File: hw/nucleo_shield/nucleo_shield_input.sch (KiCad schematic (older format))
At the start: 57 parts, among them P1 CONN_INH1, P17 CONN_INH3, P5 CONN_INH2, U15 LTV-847, U16 LTV-847, U3 LTV-847, U4 LTV-847, U5 LTV-847, U6 LTV-847

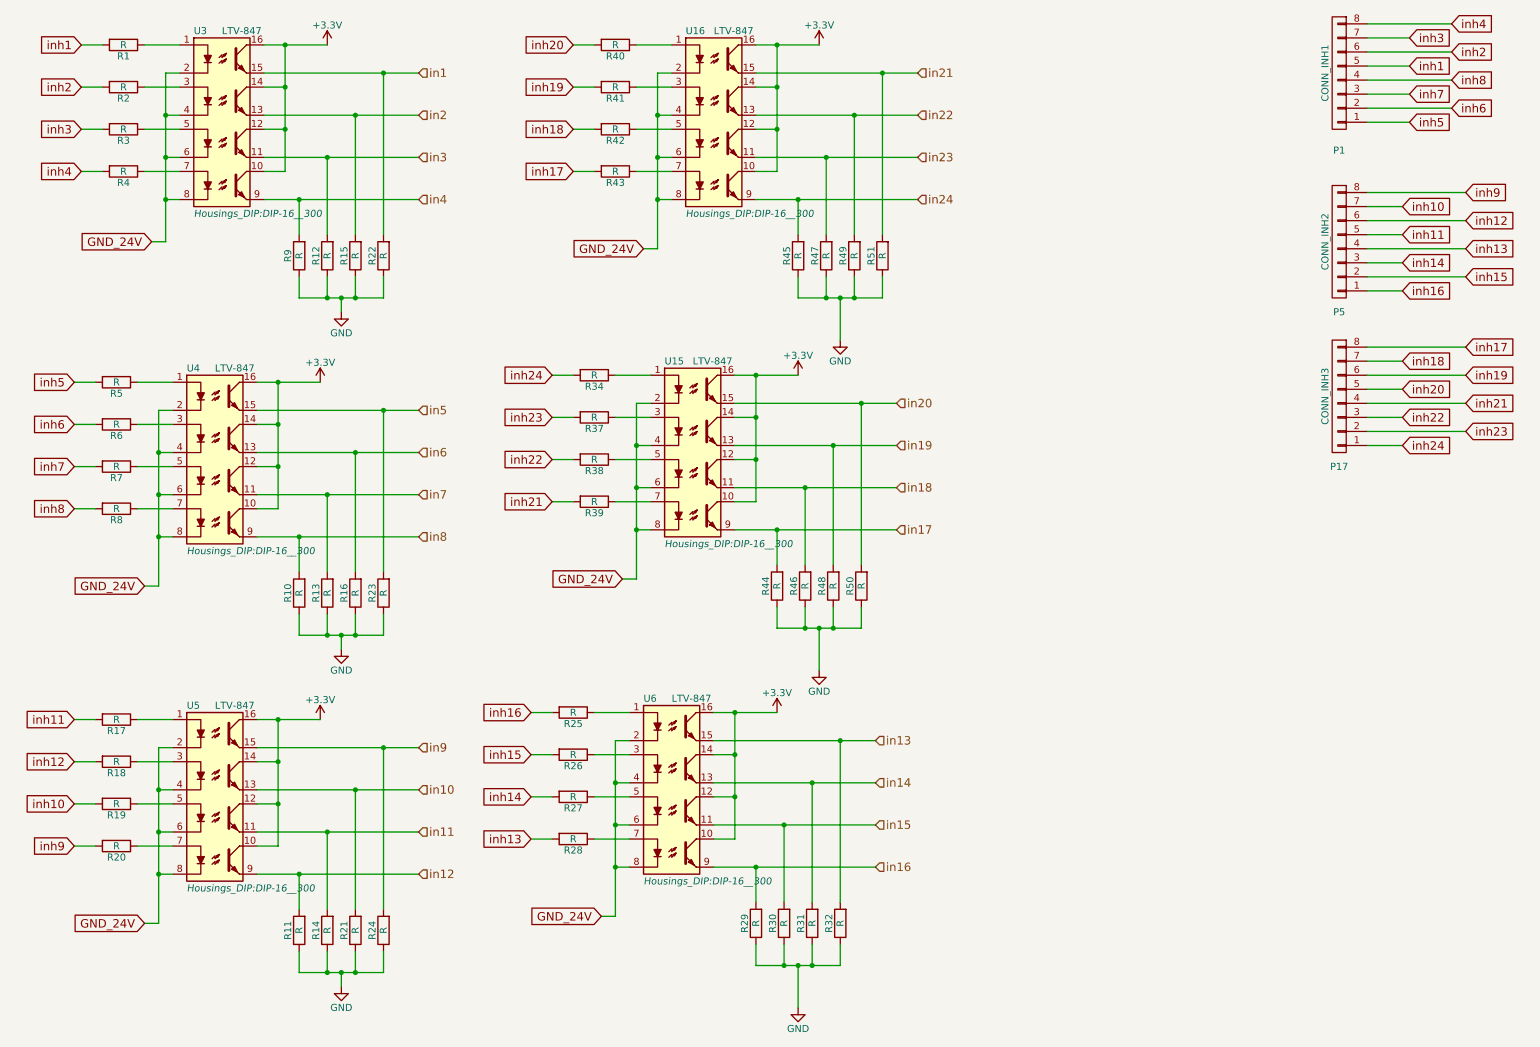
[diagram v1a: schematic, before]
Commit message: Nucleo: Remove input pullup on pcf
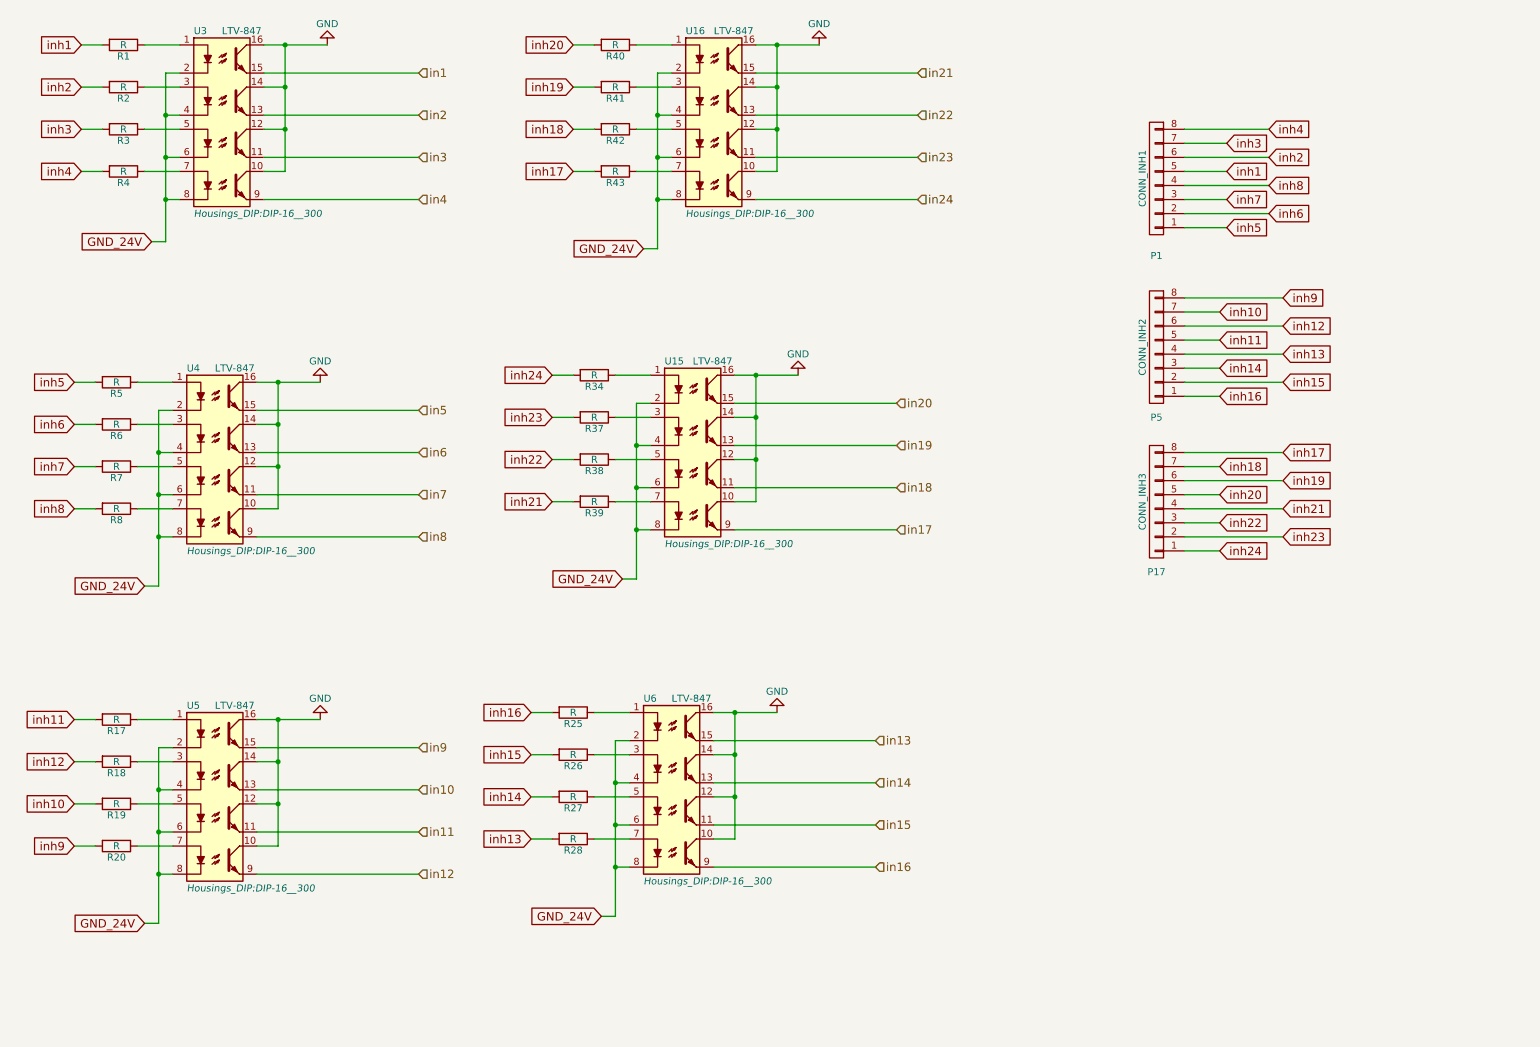
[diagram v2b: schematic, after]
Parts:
- removed R10, R11, R12, R13, R14, R15, R16, R21, R22, R23, R24, R29, R30, R31, R32, R44, R45, R46, R47, R48, R49, R50, R51, R9: R, Resistors_SMD:R_0805_HandSoldering, symbol R
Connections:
- net +3V3 is gone; now on net GND: U15.10, U15.12, U15.14, U15.16, U16.10, U16.12, U16.14, U16.16, U3.10, U3.12, U3.14, U3.16, U4.10, U4.12, U4.14, U4.16, U5.10, U5.12, U5.14, U5.16, U6.10, U6.12, U6.14, U6.16
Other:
- moved on the sheet: P1, P17, P5

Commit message: HW: fix nucleo inputs without pull ups
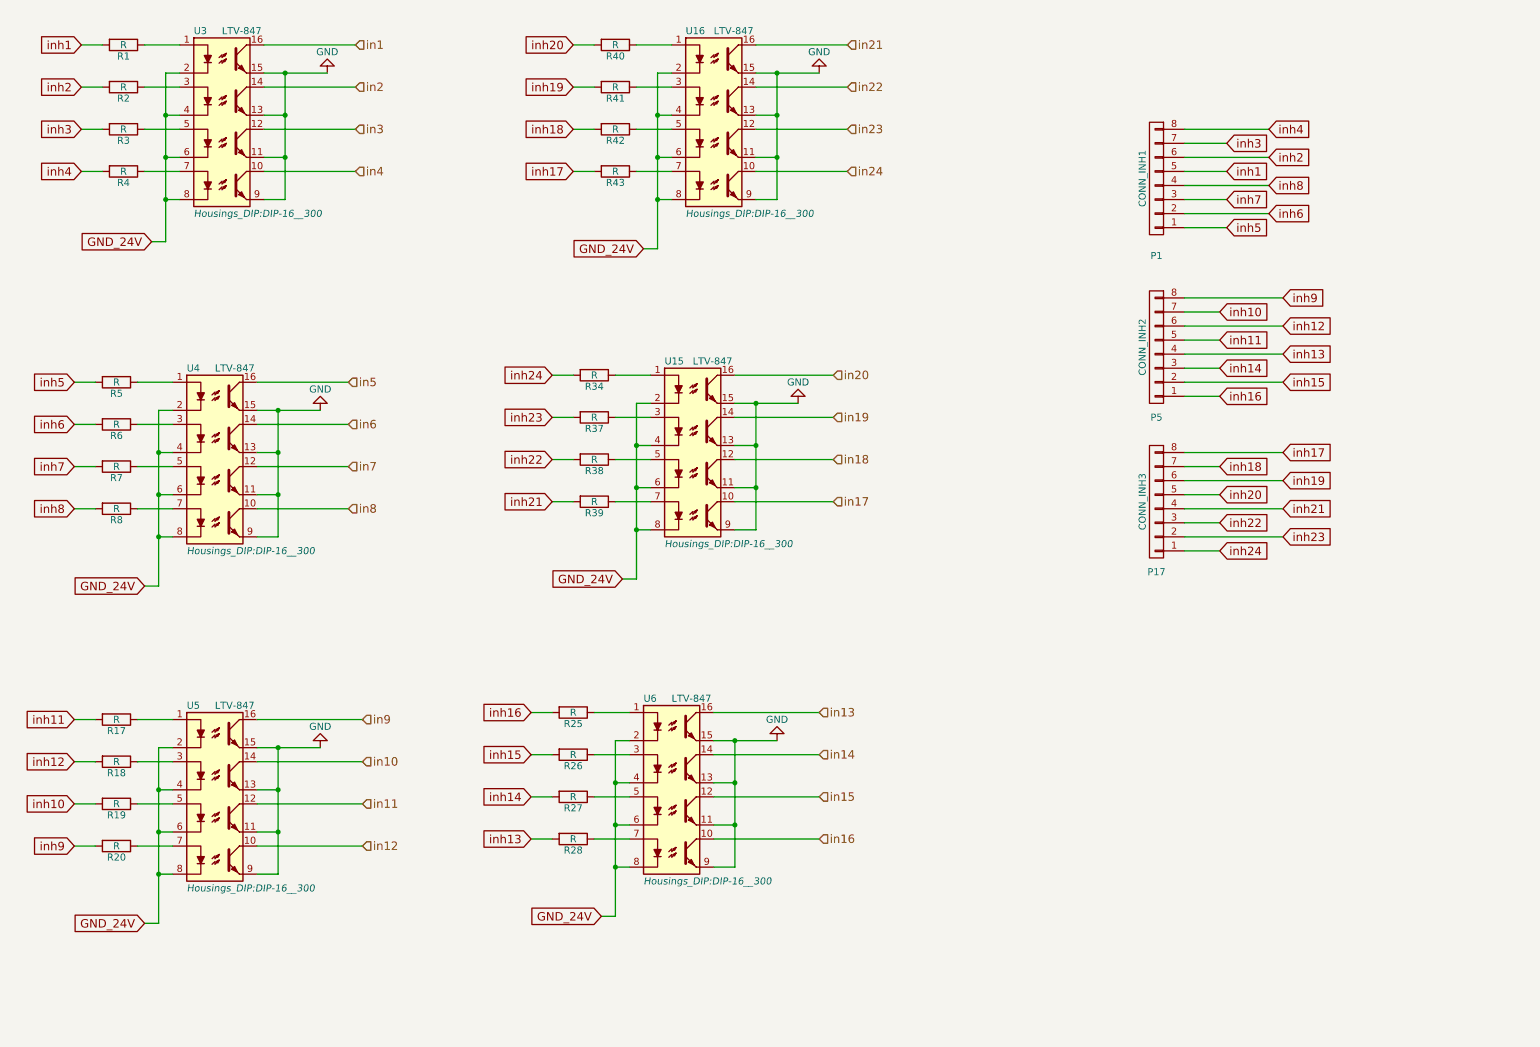
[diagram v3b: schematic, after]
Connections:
- net GND: now also U15.11, U15.13, U15.15, U15.9, U16.11, U16.13, U16.15, U16.9, U3.11, U3.13, U3.15, U3.9, U4.11, U4.13, U4.15, U4.9, U5.11, U5.13, U5.15, U5.9, U6.11, U6.13, U6.15, U6.9; no longer U15.10, U15.12, U15.14, U15.16, U16.10, U16.12, U16.14, U16.16, U3.10, U3.12, U3.14, U3.16, U4.10, U4.12, U4.14, U4.16, U5.10, U5.12, U5.14, U5.16, U6.10, U6.12, U6.14, U6.16
- net in1: now also U3.16; no longer U3.15
- net in10: now also U5.14; no longer U5.13
- net in11: now also U5.12; no longer U5.11
- net in12: now also U5.10; no longer U5.9
- net in13: now also U6.16; no longer U6.15
- net in14: now also U6.14; no longer U6.13
- net in15: now also U6.12; no longer U6.11
- net in16: now also U6.10; no longer U6.9
- net in17: now also U15.10; no longer U15.9
- net in18: now also U15.12; no longer U15.11
- net in19: now also U15.14; no longer U15.13
- net in2: now also U3.14; no longer U3.13
- net in20: now also U15.16; no longer U15.15
- net in21: now also U16.16; no longer U16.15
- net in22: now also U16.14; no longer U16.13
- net in23: now also U16.12; no longer U16.11
- net in24: now also U16.10; no longer U16.9
- net in3: now also U3.12; no longer U3.11
- net in4: now also U3.10; no longer U3.9
- net in5: now also U4.16; no longer U4.15
- net in6: now also U4.14; no longer U4.13
- net in7: now also U4.12; no longer U4.11
- net in8: now also U4.10; no longer U4.9
- net in9: now also U5.16; no longer U5.15
